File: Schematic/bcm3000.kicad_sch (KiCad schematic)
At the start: 13 parts, among them SW1 SW_Push, SW2 SW_Push, U1 MCP6002-I/P, U2 SBC-LCD16x2

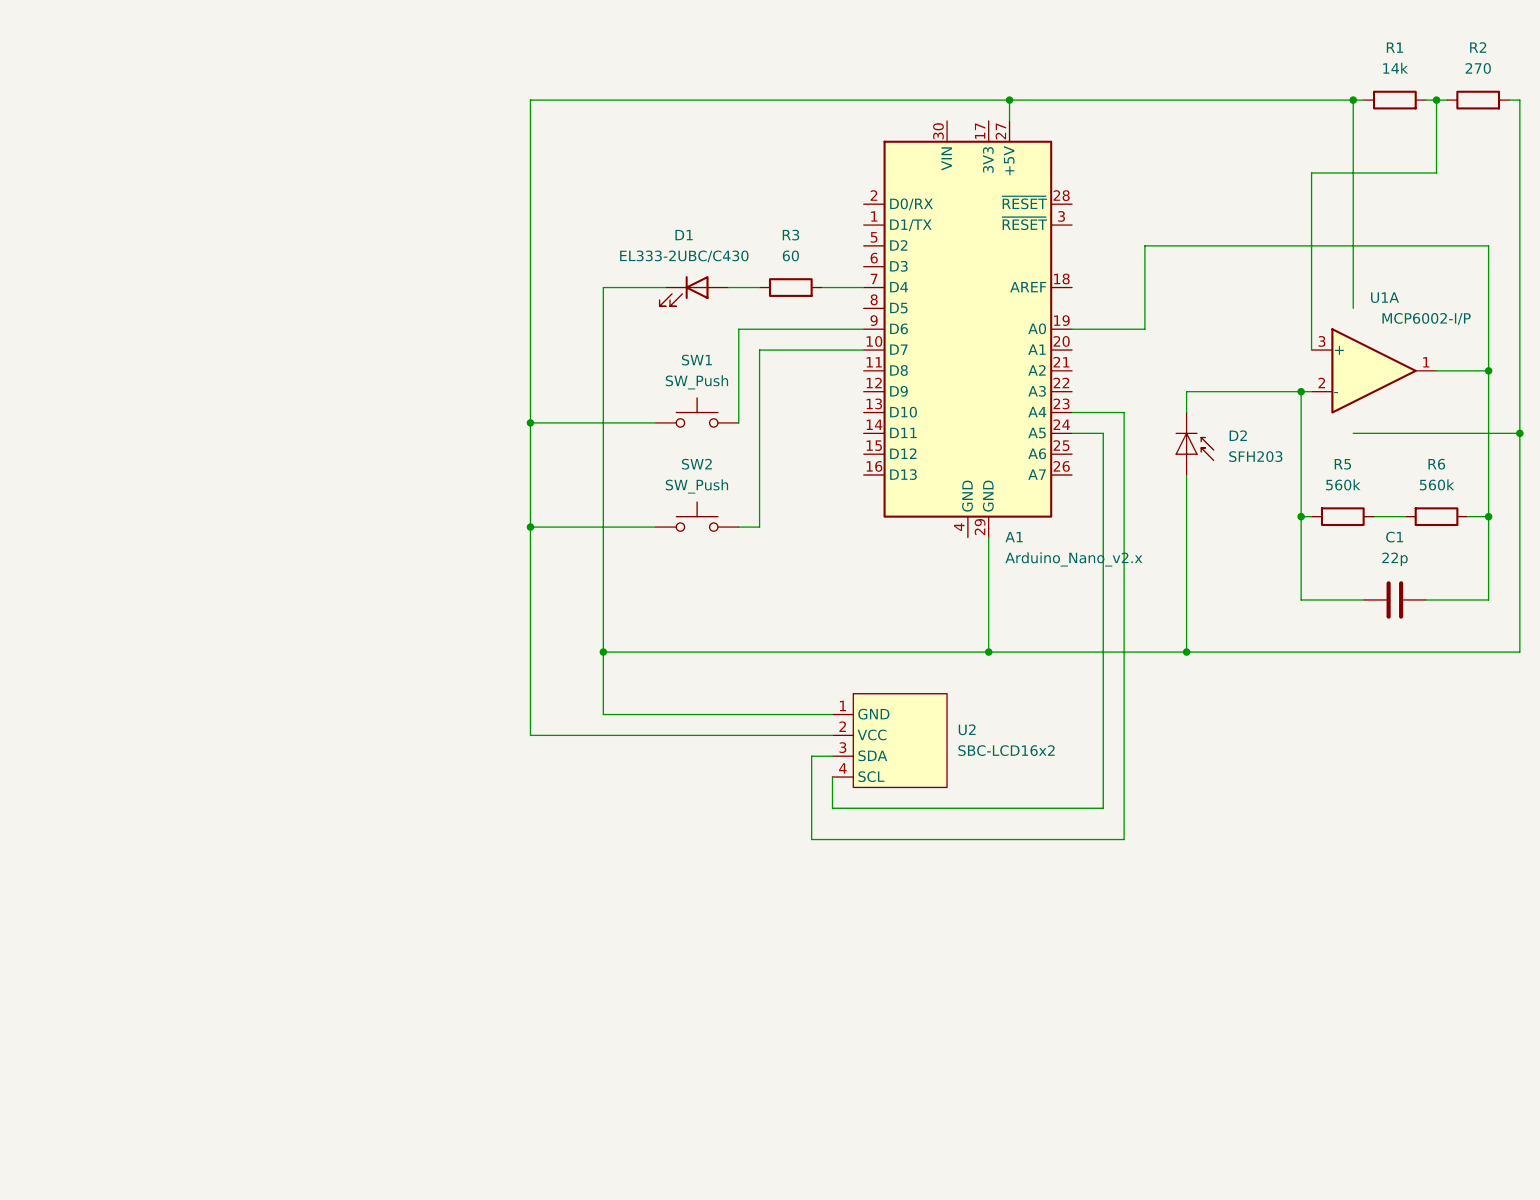
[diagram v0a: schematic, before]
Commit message: added capacitors, disabled 2nd op amp
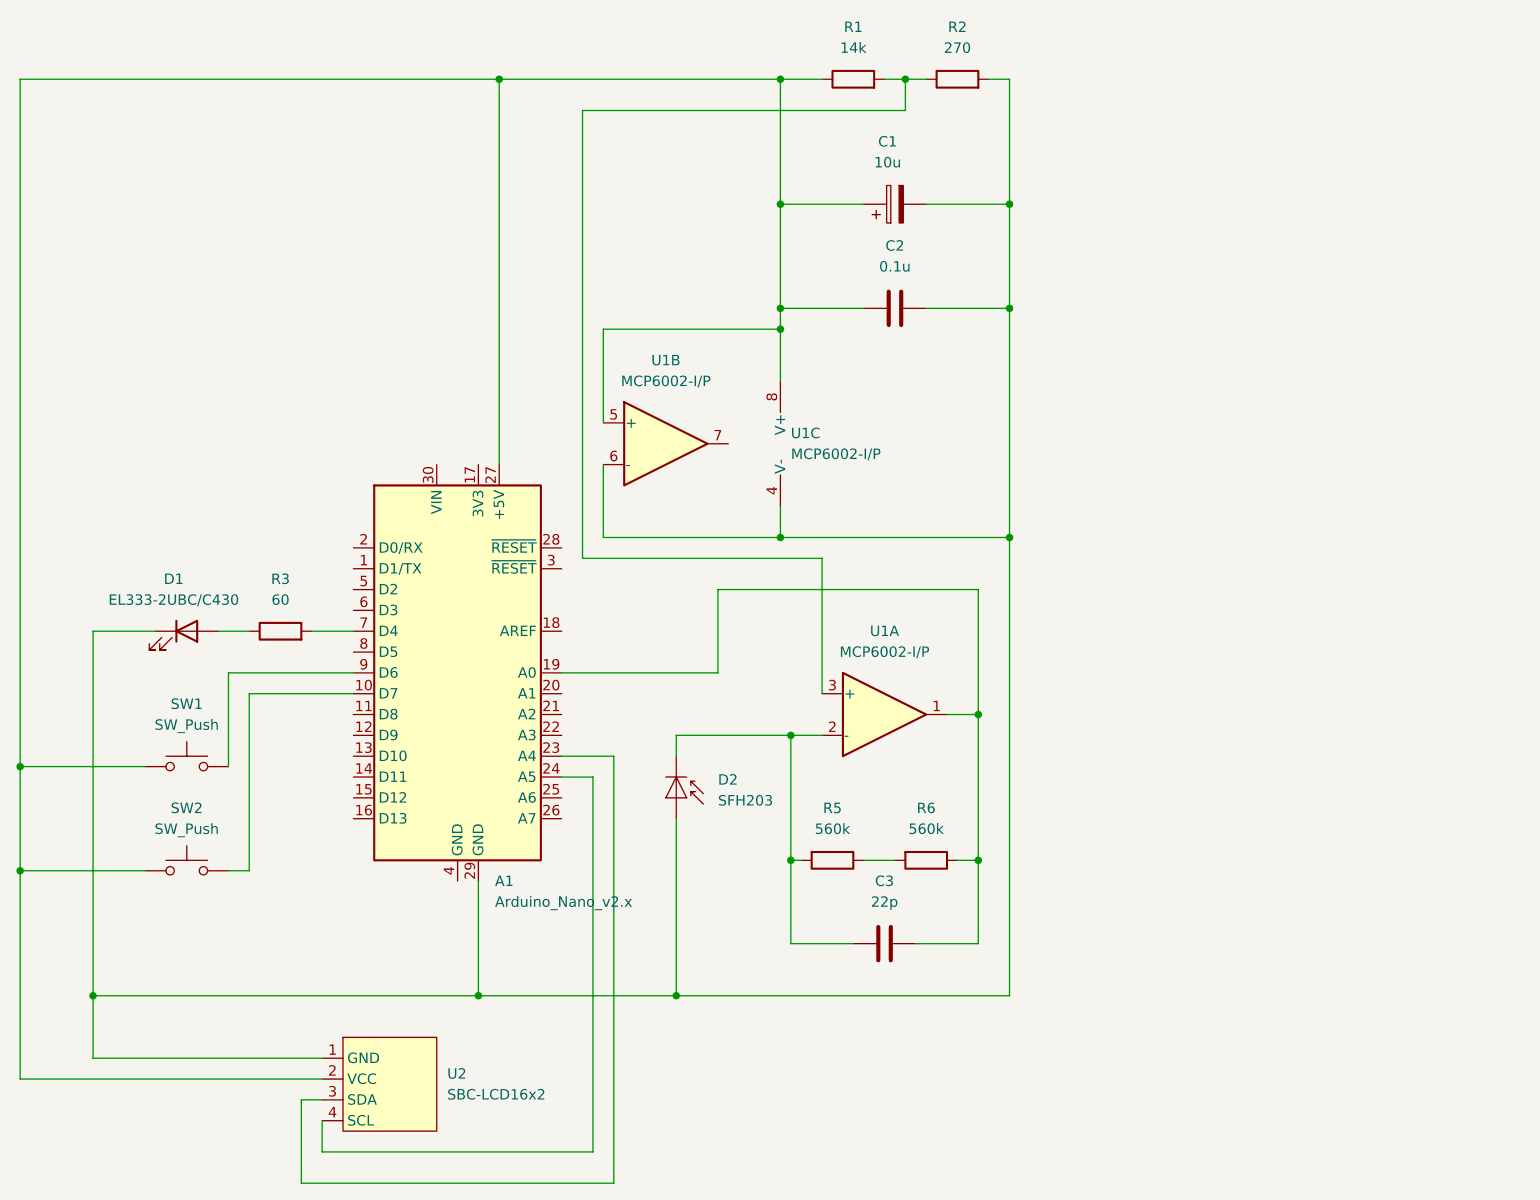
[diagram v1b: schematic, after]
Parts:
- added C1: 10u, symbol Device:C_Polarized
- added C2: 0.1u, symbol Device:C
- added unit 3 of U1
- added unit 2 of U1
- renumbered C1 to C3
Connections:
- net at A1.27 (+5V), R1.1, SW1.1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: now also C1.1, C2.1, U1.5 (+), U1.8 (V+)
- net at A1.29 (GND), D1.1 (K), D2.2 (A)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: now also C1.2, C2.2, U1.4 (V-), U1.6 (-)
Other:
- moved on the sheet: A1, C3, D1, D2, R1, R2, R3, R5, R6, SW1, SW2, U2
